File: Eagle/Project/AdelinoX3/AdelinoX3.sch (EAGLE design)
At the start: 80 parts, among them J1 DC-044-A, J2 YELLOW-8P-2.54, J3 YELLOW-6P-2.54, J4 YELLOW-8P-2.54, J5 YELLOW-8P-2.54, J6 4P-2.0, J7 YELLOW-2X3P-2.54, J8 4P-2.0, Q1 NCE3407A, Q2 CJ2305, SW1 TS-1101F, U1 CJT1117-3.3-SOT223, U2 MP1496DJ-SOT23-8, U3 ESP-12F / OPL: 317060163 / SM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, U4 DNP, U5 ATMEGA32U4-MUR-QFN44, U6 DNP, X1 306010049_XTAL_16MHZ-3225_4P

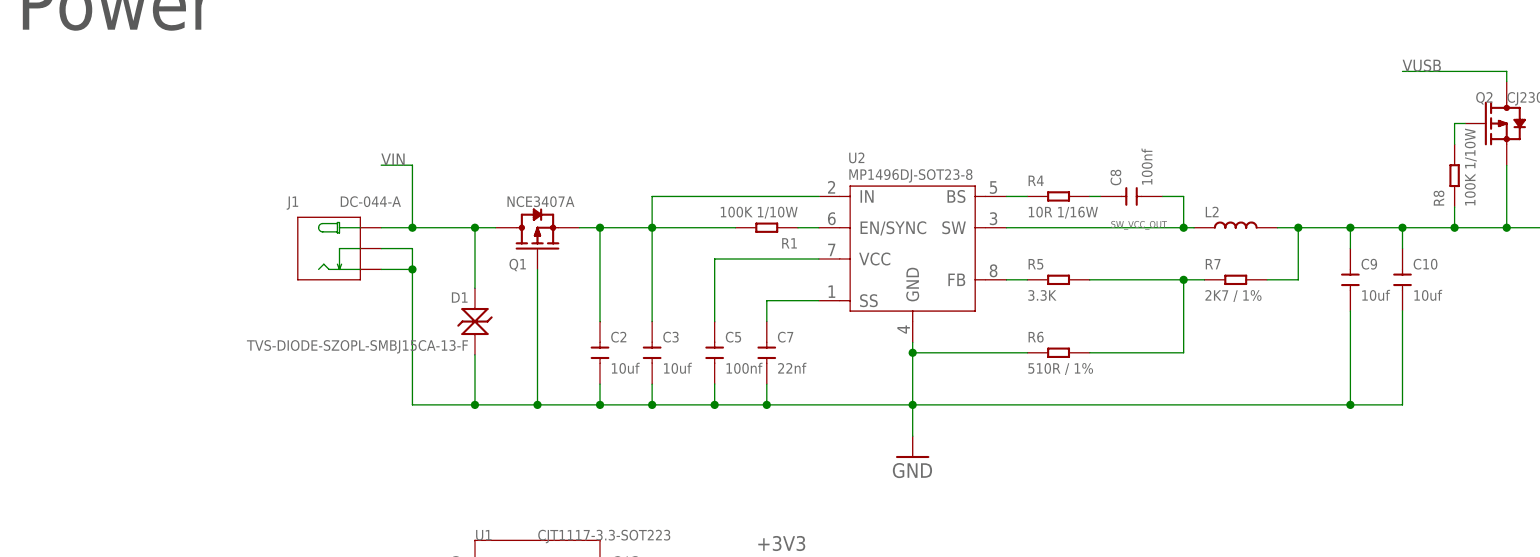
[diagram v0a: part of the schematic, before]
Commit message: Wip; use same parts as Seeeduino for SPS.
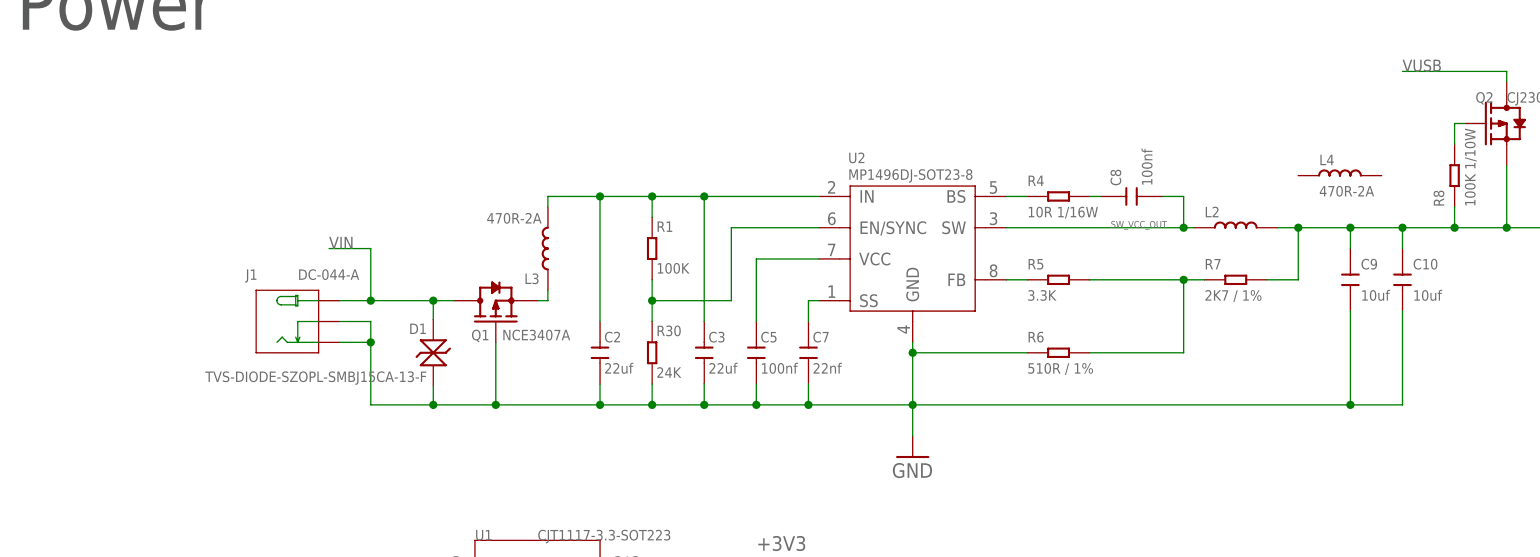
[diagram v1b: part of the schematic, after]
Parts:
- added L3, L4: 470R-2A, OPL_Ferrite_and_Magnetic_Bead:SMD-FERRITE-BEAD-470R-2A(0805)'0805'
- added R30: 24K, Seeed-Resistor:SMD-RES-24K-1%-1/10W(0603)
- C2, C3: value 10uf -> 22uf; device Seeed-Capacitor:CERAMIC-10UF-25V-10%-X5R(0805) -> Seeed-Capacitor:CERAMIC-22UF-16V-10%-X7R(1206)
- R1: value 100K 1/10W -> 100K
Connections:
- removed net SW_EN: R1.1, U2.EN/SYNC
- new net N$7: R1.2, R30.2, U2.EN/SYNC
- new net N$8: L3.1, Q1.S
- net GND: now also R30.1
- net SW_VCC_IN: now also L3.2, R1.1; no longer Q1.S, R1.2
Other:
- moved on the sheet: C3, C5, C7, D1, J1, Q1, R1

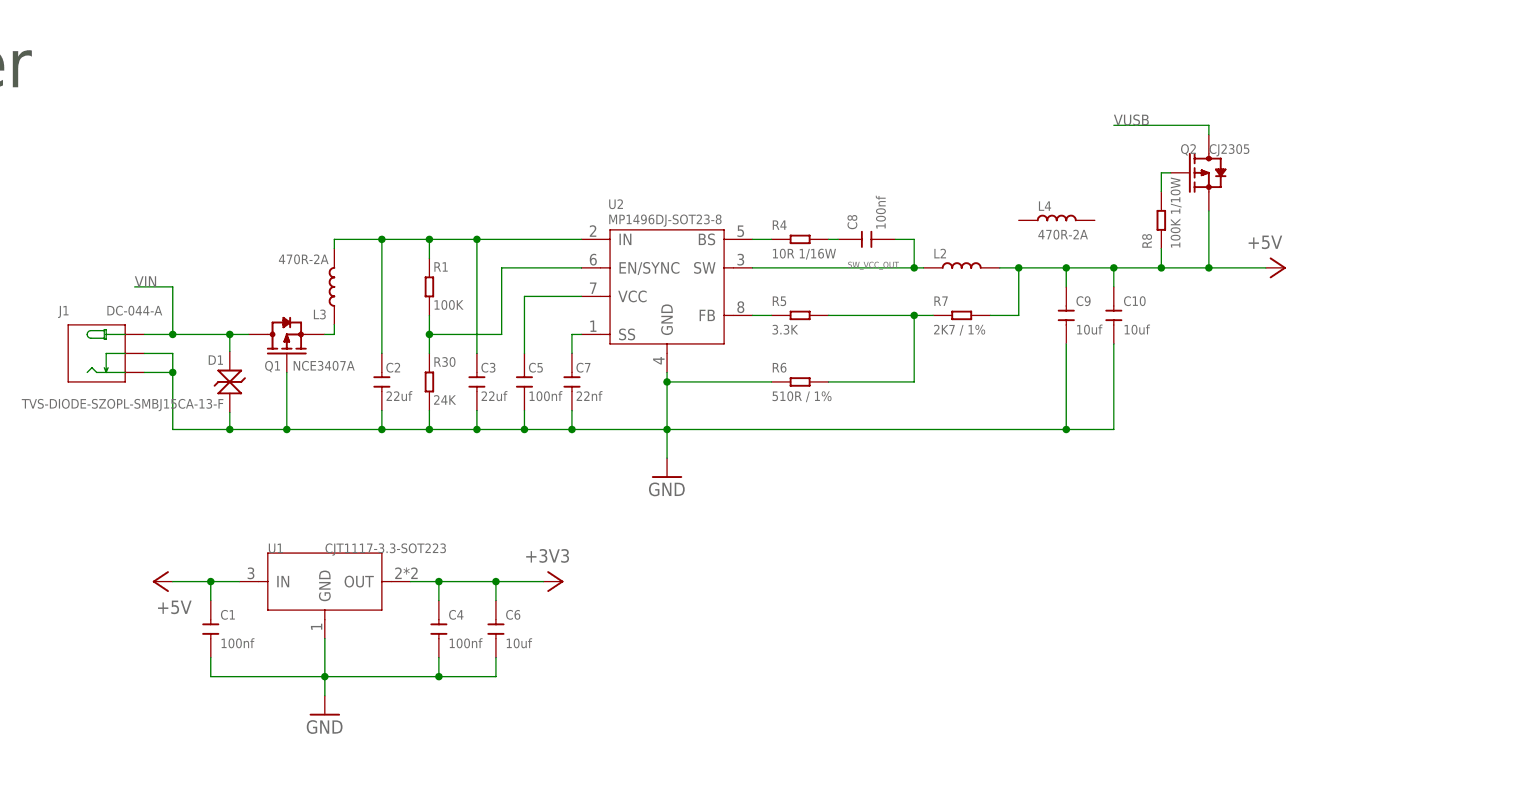
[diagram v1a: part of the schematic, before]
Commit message: Schematic changes to 0603 done.
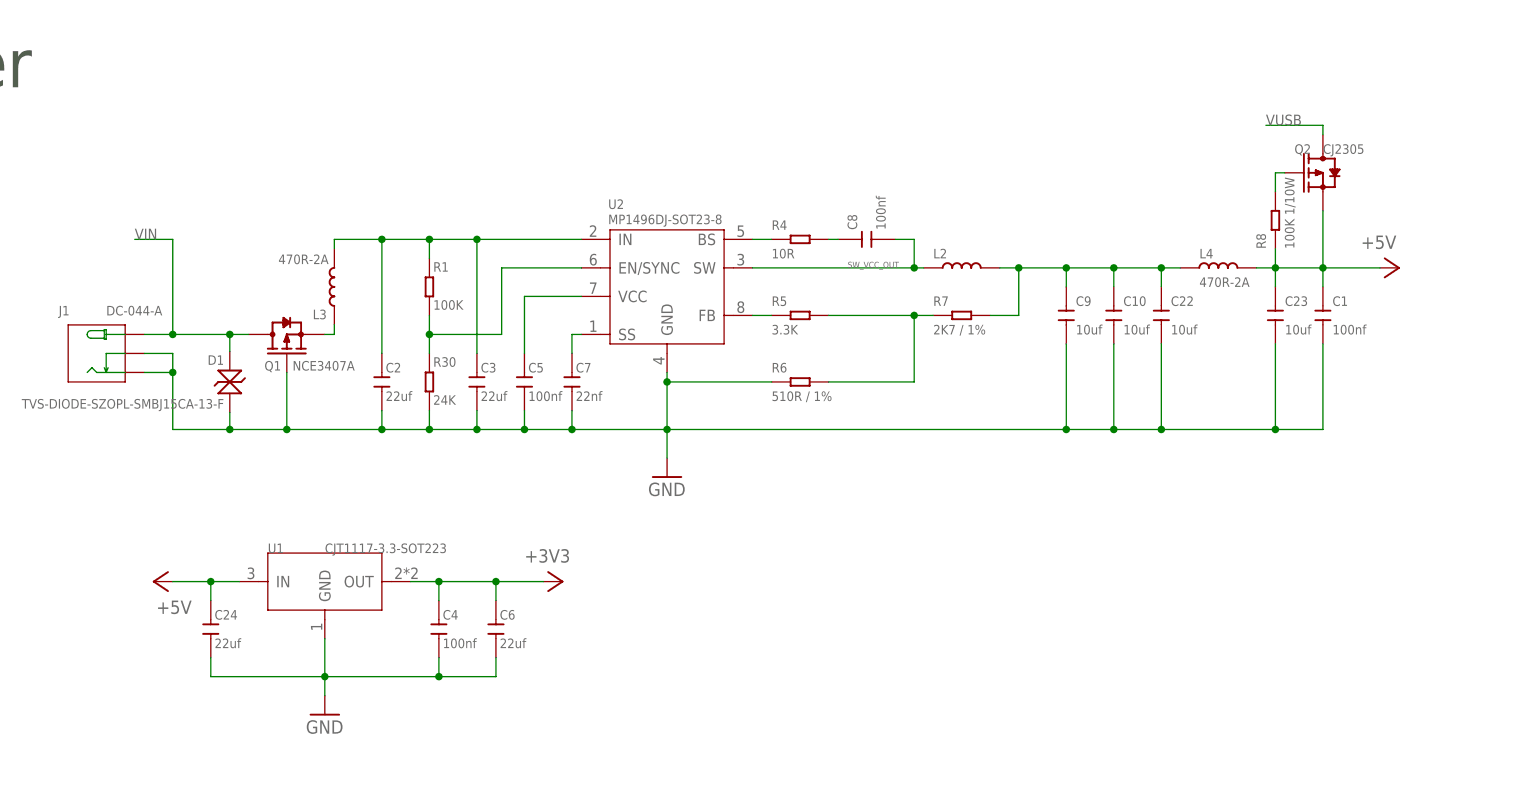
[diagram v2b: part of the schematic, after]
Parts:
- added C22, C23: 10uf, Seeed-Capacitor:CERAMIC-10UF-25V-10%-X5R(0805)
- added C24: 22uf, Seeed-Capacitor:CERAMIC-22UF-16V-10%-X7R(1206)
- C6: value 10uf -> 22uf; device Seeed-Capacitor:CERAMIC-10UF-25V-10%-X5R(0805) -> OPL_Capacitor:CERAMIC-22UF-16V-10%-X7R(1206)
- R28: device Seeed-Resistor:SMD-RES-470R-5%-1/16W(0402) -> Seeed-Resistor:SMD-RES-470R-5%-1/10W(0603)
- R4: value 10R 1/16W -> 10R; device Seeed-Resistor:SMD-RES-10R-1%-1/16W(0402) -> Seeed-Resistor:SMD-RES-10R-1%-1/10W(0603)
- R5: device Seeed-Resistor:SMD-RES-3.3K-5%-1/16W(0402) -> Seeed-Resistor:SMD-RES-3.3K-5%-1/10W(0603)
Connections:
- new net N$10: C10.2, C22.2, C9.2, L2.2, L4.1, R7.2
- net +5V: now also C23.2, C24.2, L4.2; no longer C10.2, C9.2, L2.2, R7.2
- net GND: now also C22.1, C23.1, C24.1
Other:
- moved on the sheet: C1, L4, Q2, R8

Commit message: First X3 routing finished.
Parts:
- removed C4: 100nf, OPL_Capacitor:CERAMIC-100NF-50V-10%-X7R(0603)
- added TP1, TP10, TP11, TP12, TP13, TP14, TP15, TP16, TP17, TP2, TP3, TP4, TP5, TP6, TP7, TP8, TP9: TPTP16R, testpad:TPTP16R
- D7: LABEL WIFI -> ESP
- R10, R20, R8, R9: value 100K 1/10W -> 100K
- R11, R13, R14, R23, R29: value 10K 1/10W -> 10K
- R12: value 1M 1/10W -> 1M
- R15, R16, R17, R21, R22, R24, R25, R26, R27: value 1K 1/10W -> 1K
- U1: value CJT1117-3.3-SOT223 -> CJT1117-3.3
- U3: device Seeed-OPL-2017-01-Sensor-camilo:ESP-12F -> Adelino-Misc:ESP-12F
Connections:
- net N$10 renamed SW_F1
- net N$12 renamed GPIO12
- net N$14 renamed GPIO13
- net N$17 renamed TXD
- net N$18 renamed RXD
- net N$19 renamed GPIO14
- net N$20 renamed GPIO15
- net N$22 renamed RST
- net N$5 renamed GPIO16
- net N$6 renamed _ACT
- removed net N$1: ESD1.IO2, R2.1, USB1.DM
- removed net N$2: ESD1.IO1, R3.1, USB1.DP
- removed net N$4: D7.+, R28.2
- removed net N$9: ESD1.VCC, F1.1, USB1.VCC
- new net UD+: ESD1.IO1, R3.1, TP7.TP, USB1.DP
- new net UD-: ESD1.IO2, R2.1, TP6.TP, USB1.DM
- new net UVCC: ESD1.VCC, F1.1, TP5.TP, USB1.VCC
- new net _ESP: D7.-, R28.1
- net +3V3: now also D7.+, TP16.TP; no longer C4.2, R28.1
- net +5V: now also TP17.TP
- net AT_MISO: now also TP1.TP
- net AT_MOSI: now also TP4.TP
- net AT_SCK: now also TP2.TP
- net GND: now also TP10.TP; no longer C4.1
- net GPIO2_LED: now also R28.2; no longer D7.-
- net PIN_D0: now also TP12.TP
- net PIN_D1: now also TP13.TP
- net PIN_D2_SDA: now also TP14.TP
- net PIN_D3_SCL: now also TP15.TP
- net RESET: now also TP3.TP
- net RSTAT: now also TP11.TP
- net UGND: now also TP8.TP
- net VIN: now also TP9.TP
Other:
- moved on the sheet: C2, C24, C3, C6, D5, D7, J6, J8, R1, R28, R30, U1

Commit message: Parts renumbered; tidy up silkscreen.
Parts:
- removed C24: 22uf, Seeed-Capacitor:CERAMIC-22UF-16V-10%-X7R(1206)
- added C4: 22uf, Seeed-Capacitor:CERAMIC-22UF-16V-10%-X7R(1206)
- C1: value 100nf -> 22uf; device OPL_Capacitor:CERAMIC-100NF-50V-10%-X7R(0603) -> Seeed-Capacitor:CERAMIC-22UF-16V-10%-X7R(1206)
- C11, C8: value 100nf -> 10uf; device OPL_Capacitor:CERAMIC-100NF-50V-10%-X7R(0603) -> Seeed-Capacitor:CERAMIC-10UF-25V-10%-X5R(0805)
- C12, C13: value 22pf -> 100nf; device Seeed-Capacitor:CERAMIC-22PF-50V-5%-NPO(0603) -> OPL_Capacitor:CERAMIC-100NF-50V-10%-X7R(0603)
- C14, C15: value 100nf -> 22pf; device OPL_Capacitor:CERAMIC-100NF-50V-10%-X7R(0603) -> Seeed-Capacitor:CERAMIC-22PF-50V-5%-NPO(0603)
- C20: value 1uf -> 100nf; device Seeed-Capacitor:CERAMIC-1UF-25V-10%-X7R(0603) -> OPL_Capacitor:CERAMIC-100NF-50V-10%-X7R(0603)
- C21: device Seeed-Capacitor:CERAMIC-100NF-50V-10%-X7R(0603) -> OPL_Capacitor:CERAMIC-100NF-50V-10%-X7R(0603)
- C22: value 10uf -> 1uf; device Seeed-Capacitor:CERAMIC-10UF-25V-10%-X5R(0805) -> Seeed-Capacitor:CERAMIC-1UF-25V-10%-X7R(0603)
- C23: value 10uf -> 100nf; device Seeed-Capacitor:CERAMIC-10UF-25V-10%-X5R(0805) -> Seeed-Capacitor:CERAMIC-100NF-50V-10%-X7R(0603)
- C3: device Seeed-Capacitor:CERAMIC-22UF-16V-10%-X7R(1206) -> OPL_Capacitor:CERAMIC-22UF-16V-10%-X7R(1206)
- C6: value 22uf -> 22nf; device OPL_Capacitor:CERAMIC-22UF-16V-10%-X7R(1206) -> Seeed-Capacitor:CERAMIC-22NF-50V-10%-X7R(0603)
- C7: value 22nf -> 100nf; device Seeed-Capacitor:CERAMIC-22NF-50V-10%-X7R(0603) -> OPL_Capacitor:CERAMIC-100NF-50V-10%-X7R(0603)
- D3: value GRE-0603 -> 20V-500MA; device Seeed-LED:SMD-LED-CLEAR-GREEN(0603) -> Seeed-Diode:SMD-DIODE-SCHOTTKY-20V-500MA(SOD-123)P; LABEL PWR -> (none)
- D4: value YEL-0603 -> BLU-0603; device Seeed-LED:SMD-LED-CLEAR-YELLOW(0603) -> Seeed-LED:SMD-LED-CLEAR-BLUE(0603); LABEL ACT -> ESP
- D5: value 20V-500MA -> GRE-0603; device Seeed-Diode:SMD-DIODE-SCHOTTKY-20V-500MA(SOD-123)P -> Seeed-LED:SMD-LED-CLEAR-GREEN(0603); LABEL (none) -> PWR
- D6: LABEL D13 -> ACT
- D7: value BLU-0603 -> YEL-0603; device Seeed-LED:SMD-LED-CLEAR-BLUE(0603) -> Seeed-LED:SMD-LED-CLEAR-YELLOW(0603); LABEL ESP -> D13
- L1: value 330R-1500MA -> 470R-2A; device Seeed-Inductor:SMD-FERRITE-BEAD-330R-1500MA(0805)'0805' -> OPL_Ferrite_and_Magnetic_Bead:SMD-FERRITE-BEAD-470R-2A(0805)'0805'
- L2: value 10UH-225MA -> 330R-1500MA; device Seeed-Inductor:SMD-INDUCTOR-10UH-20%-2.35A(2P-5X5X4MM) -> Seeed-Inductor:SMD-FERRITE-BEAD-330R-1500MA(0805)'0805'
- L3: value 470R-2A -> 10UH-225MA; device OPL_Ferrite_and_Magnetic_Bead:SMD-FERRITE-BEAD-470R-2A(0805)'0805' -> Seeed-Inductor:SMD-INDUCTOR-10UH-20%-2.35A(2P-5X5X4MM)
- R11: value 10K -> 100K; device Seeed-Resistor:SMD-RES-10K-5%-1/10W(0603) -> Seeed-Resistor:SMD-RES-100K-5%-1/10W(0603)
- R12: value 1M -> 10K; device Seeed-Resistor:SMD-RES-1M-5%-1/10W(0603) -> Seeed-Resistor:SMD-RES-10K-5%-1/10W(0603)
- R13: value 10K -> 1M; device Seeed-Resistor:SMD-RES-10K-5%-1/10W(0603) -> Seeed-Resistor:SMD-RES-1M-5%-1/10W(0603)
- R15, R24: value 1K -> 10K; device Seeed-Resistor:SMD-RES-1K-5%-1/10W(0603) -> Seeed-Resistor:SMD-RES-10K-5%-1/10W(0603)
- R19: value 0R -> 1K; device Seeed-Resistor:SMD-RES-0R-5%-1/10W(0603) -> Seeed-Resistor:SMD-RES-1K-5%-1/10W(0603)
- R2: value 22R -> 24K; device Seeed-Resistor:SMD-RES-22R-5%-1/10W(0603) -> Seeed-Resistor:SMD-RES-24K-1%-1/10W(0603)
- R20: value 100K -> 0R; device Seeed-Resistor:SMD-RES-100K-5%-1/10W(0603) -> Seeed-Resistor:SMD-RES-0R-5%-1/10W(0603)
- R21: value 1K -> 100K; device Seeed-Resistor:SMD-RES-1K-5%-1/10W(0603) -> Seeed-Resistor:SMD-RES-100K-5%-1/10W(0603)
- R23: value 10K -> 1K; device Seeed-Resistor:SMD-RES-10K-5%-1/10W(0603) -> Seeed-Resistor:SMD-RES-1K-5%-1/10W(0603)
- R28: value 470R -> 1K; device Seeed-Resistor:SMD-RES-470R-5%-1/10W(0603) -> Seeed-Resistor:SMD-RES-1K-5%-1/10W(0603)
- R30: value 24K -> 470R; device Seeed-Resistor:SMD-RES-24K-1%-1/10W(0603) -> Seeed-Resistor:SMD-RES-470R-5%-1/10W(0603)
- R4: value 10R -> 22R; device Seeed-Resistor:SMD-RES-10R-1%-1/10W(0603) -> Seeed-Resistor:SMD-RES-22R-5%-1/10W(0603)
- R5: value 3.3K -> 10R; device Seeed-Resistor:SMD-RES-3.3K-5%-1/10W(0603) -> Seeed-Resistor:SMD-RES-10R-1%-1/10W(0603)
- R6: value 3K / 1% -> 3.3K; device Seeed-Resistor:SMD-RES-510R-1%-1/10W(0603) -> Seeed-Resistor:SMD-RES-3.3K-5%-1/10W(0603); R 510R / 1% -> (none)
- R7: value 2K7 / 1% -> 3K / 1%; device Seeed-Resistor:SMD-RES-2.7K-1%-1/10W(0603) -> Seeed-Resistor:SMD-RES-510R-1%-1/10W(0603); R 2K7 / 1% -> 510R / 1%
- R8: value 100K -> 2K7 / 1%; device Seeed-Resistor:SMD-RES-100K-5%-1/10W(0603) -> Seeed-Resistor:SMD-RES-2.7K-1%-1/10W(0603); R (none) -> 2K7 / 1%
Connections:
- net +3V3: now also C3.2, D4.+, R15.1, R24.2; no longer C6.2, D7.+, R13.1, R23.2
- net +5V: now also C11.2, C12.2, C19.1, C20.1, C23.1, D3.-, R10.1, R11.2, R25.1; no longer C15.1, C16.1, C21.1, C23.2, C24.2, D2.-, R10.2, R24.1, R8.1
- net ACT_LED: now also R26.1; no longer R25.1
- net AT_MISO: now also R16.1; no longer R15.1
- net AT_MOSI: now also R17.1; no longer R16.1
- net AT_SCK: now also R18.1; no longer R17.1
- net AT_SS: now also D2.+, R19.1; no longer D5.+, R18.1
- net BOOT_MODE: now also R24.1, R28.2; no longer R23.1, R27.2
- net D+: now also R4.2; no longer R3.2
- net D-: now also R3.2; no longer R2.2
- net ESP_EN: now also R15.2; no longer R14.2
- net GND: now also C11.1, C14.1, C15.1, C20.2, C23.2, C4.1, C8.1, D5.-, D7.-, L2.1, R2.1, R21.1, R7.1; no longer C13.1, C14.2, C15.2, C22.1, C23.1, C24.1, C7.1, D3.-, D4.-, L1.1, R20.1, R30.1, R6.1
- net GPIO12: now also R16.2; no longer R15.2
- net GPIO13: now also R17.2; no longer R16.2
- net GPIO14: now also R18.2; no longer R17.2
- net GPIO15: now also R19.2, R21.2; no longer R18.2, R20.2
- net GPIO16: now also R20.2; no longer R19.2
- net GPIO2_LED: now also R30.2; no longer R28.2
- net N$13: now also C16.1, R12.2; no longer C14.1, R11.2
- net N$15: now also C7.2, R5.2; no longer C8.2, R4.2
- net N$23: now also R7.2, R8.1; no longer R5.2, R7.1
- net N$3: now also R9.2; no longer R8.2
- net N$7: now also R2.2; no longer R30.2
- net N$8: now also L1.1; no longer L3.1
- net PIN_AREF: now also C21.1; no longer C19.1
- net PIN_D0: now also R22.2; no longer R21.2
- net PIN_D1: now also R23.2; no longer R22.2
- net PIN_D13: now also R28.1; no longer R26.1
- net RESET: now also C13.1, D3.+, R12.1, R20.1; no longer C11.1, D2.+, R10.1, R19.1
- net RST: now also R14.2; no longer R13.2
- net RSTAT: now also C13.2, D2.-, R10.2; no longer C11.2, D5.-, R9.2
- net RXD: now also R23.1; no longer R22.1
- net SW_BS: now also R5.1; no longer R4.1
- net SW_F1: now also C8.2, L3.2, R8.2; no longer C22.2, L2.2, R7.2
- net SW_FB: now also R6.1; no longer R5.1
- net SW_SS: now also C6.2; no longer C7.2
- net SW_VCC_IN: now also C4.2, L1.2; no longer C3.2, L3.2
- net SW_VCC_OUT: now also C7.1, L3.1; no longer C8.1, L2.1
- net TXD: now also R22.1; no longer R21.1
- net UCAP: now also C22.2; no longer C20.2
- net UD+: now also R4.1; no longer R3.1
- net UD-: now also R3.1; no longer R2.1
- net UGND: now also C22.1, L2.2; no longer C20.1, L1.2
- net XTAL1: now also C14.2, R13.2; no longer C12.2, R12.2
- net XTAL2: now also C15.2, R13.1; no longer C13.2, R12.1
- net _ACT: now also D6.+, R26.2; no longer D4.+, R25.2
- net _D13: now also D7.+, R27.2; no longer D6.+, R26.2
- net _ESP: now also D4.-, R30.1; no longer D7.-, R28.1
- net _PWR: now also D5.+, R25.2; no longer D3.+, R24.2
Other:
- moved on the sheet: C1, C10, C11, C12, C13, C14, C15, C16, C17, C18, C19, C20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

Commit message: Add sensing pads; close vias; better test pad spacing.
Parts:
- added TP18, TP19: TPTP16R, testpad:TPTP16R
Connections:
- net GND: now also TP18.TP, TP19.TP
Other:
- note added: "Board sensing"
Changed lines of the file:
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@@
 <setting verticaltext="up"/>
 </settings>
-<grid distance="0.1" unitdist="inch" unit="inch" style="lines" multiple="1" display="no" altdistance="0.01" altunitdist="inch" altunit="inch"/>
+<grid distance="0.05" unitdist="inch" unit="inch" style="lines" multiple="1" display="no" altdistance="0.01" altunitdist="inch" altunit="inch"/>
 <layers>
 <layer number="1" name="Top" color="4" fill="1" visible="no" active="no"/>
@@
 <part name="TP16" library="testpad" library_urn="urn:adsk.eagle:library:385" deviceset="TP" device="TP16R" package3d_urn="urn:adsk.eagle:package:27969/1"/>
 <part name="TP17" library="testpad" library_urn="urn:adsk.eagle:library:385" deviceset="TP" device="TP16R" package3d_urn="urn:adsk.eagle:package:27969/1"/>
+<part name="TP18" library="testpad" library_urn="urn:adsk.eagle:library:385" deviceset="TP" device="TP16R" package3d_urn="urn:adsk.eagle:package:27969/1"/>
+<part name="TP19" library="testpad" library_urn="urn:adsk.eagle:library:385" deviceset="TP" device="TP16R" package3d_urn="urn:adsk.eagle:package:27969/1"/>
 </parts>
 <sheets>
@@
 <text x="13.97" y="-125.73" size="6.4516" layer="97">Security</text>
 <text x="-79.248" y="-130.556" size="2.54" layer="97">ICSP</text>
+<text x="-97.79" y="110.49" size="1.778" layer="91">Board sensing</text>
 </plain>
 <instances>
@@
 <attribute name="NAME" x="-214.63" y="108.712" size="1.4224" layer="95"/>
 <attribute name="TP_SIGNAL_NAME" x="-210.82" y="106.68" size="1.778" layer="97"/>
+</instance>
+<instance part="TP18" gate="G$1" x="-92.71" y="115.57" smashed="yes" rot="R180">
+<attribute name="NAME" x="-90.424" y="115.062" size="1.4224" layer="95" rot="R180"/>
+<attribute name="TP_SIGNAL_NAME" x="-93.98" y="116.84" size="1.778" layer="97" rot="R180"/>
+</instance>
+<instance part="TP19" gate="G$1" x="-86.36" y="115.57" smashed="yes" rot="R180">
+<attribute name="NAME" x="-84.074" y="115.062" size="1.4224" layer="95" rot="R180"/>
+<attribute name="TP_SIGNAL_NAME" x="-87.63" y="116.84" size="1.778" layer="97" rot="R180"/>
 </instance>
 </instances>
@@
 <wire x1="-212.09" y1="119.38" x2="-212.09" y2="121.92" width="0.1524" layer="91"/>
 <junction x="-212.09" y="121.92"/>
-</segment>
-<segment>
+<pinref part="TP18" gate="G$1" pin="TP"/>
+<wire x1="-92.71" y1="118.11" x2="-92.71" y2="121.92" width="0.1524" layer="91"/>
+<pinref part="TP19" gate="G$1" pin="TP"/>
+<wire x1="-86.36" y1="118.11" x2="-86.36" y2="121.92" width="0.1524" layer="91"/>
+</segment>
+<segment>
